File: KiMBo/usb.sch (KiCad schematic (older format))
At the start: 19 parts, among them U1 OSD3358, U6 TPS2051B, U7 TPD4S012, U8 74LVC2G241, U9 TPD4S012

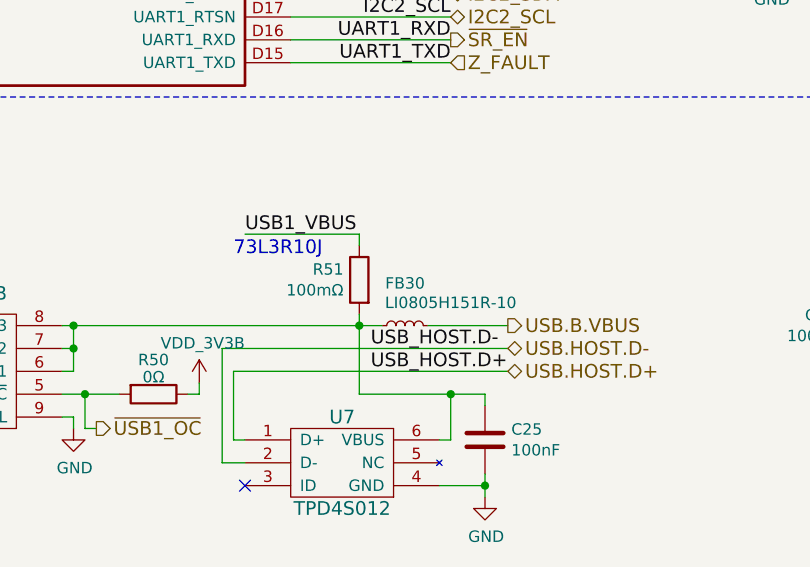
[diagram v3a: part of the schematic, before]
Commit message: Route 24V to the buck, add PTC fuse to 5V output
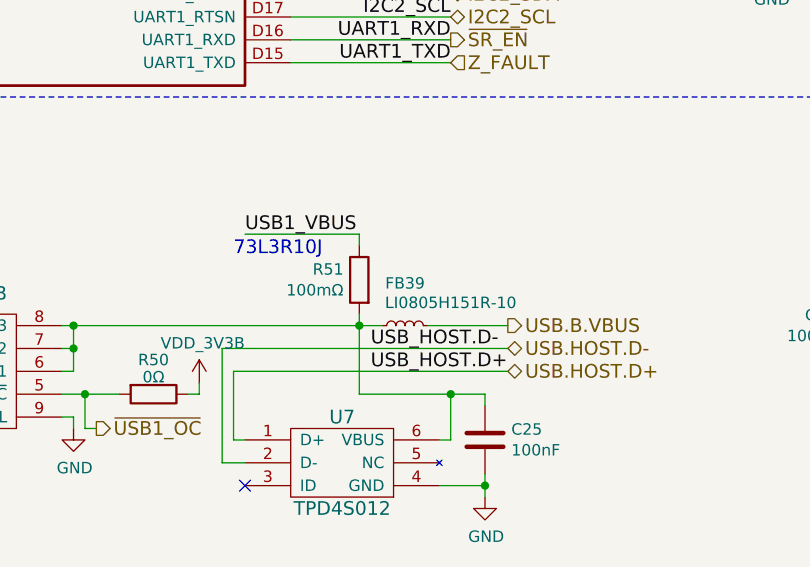
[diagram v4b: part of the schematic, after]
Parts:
- renumbered FB30 to FB39
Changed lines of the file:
@@
 USB.CLIENT.ID
 $Comp
-L INDUCTOR_Small FB30
+L INDUCTOR_Small FB39
 U 1 1 58E84972
 P 5950 4100
-F 0 "FB30" V 6135 4100 50  0000 C CNN
+F 0 "FB39" V 6135 4100 50  0000 C CNN
 F 1 "LI0805H151R-10" V 6050 3900 50  0000 C CNN
 F 2 "Resistors_SMD:R_0805" H 5950 4100 50  0001 C CNN

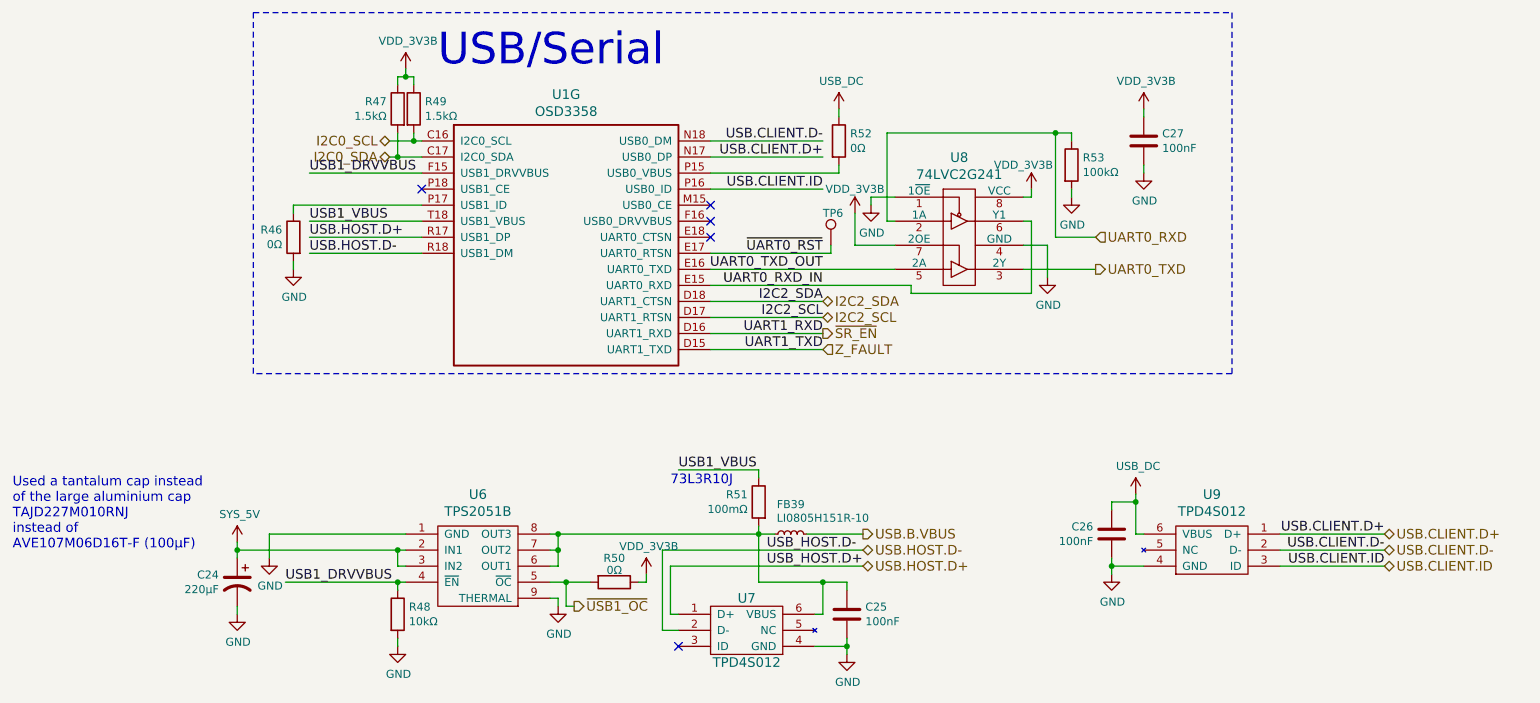
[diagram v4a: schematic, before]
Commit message: Add ferrite beads to the 5V and 3V pins at the SPI connectors
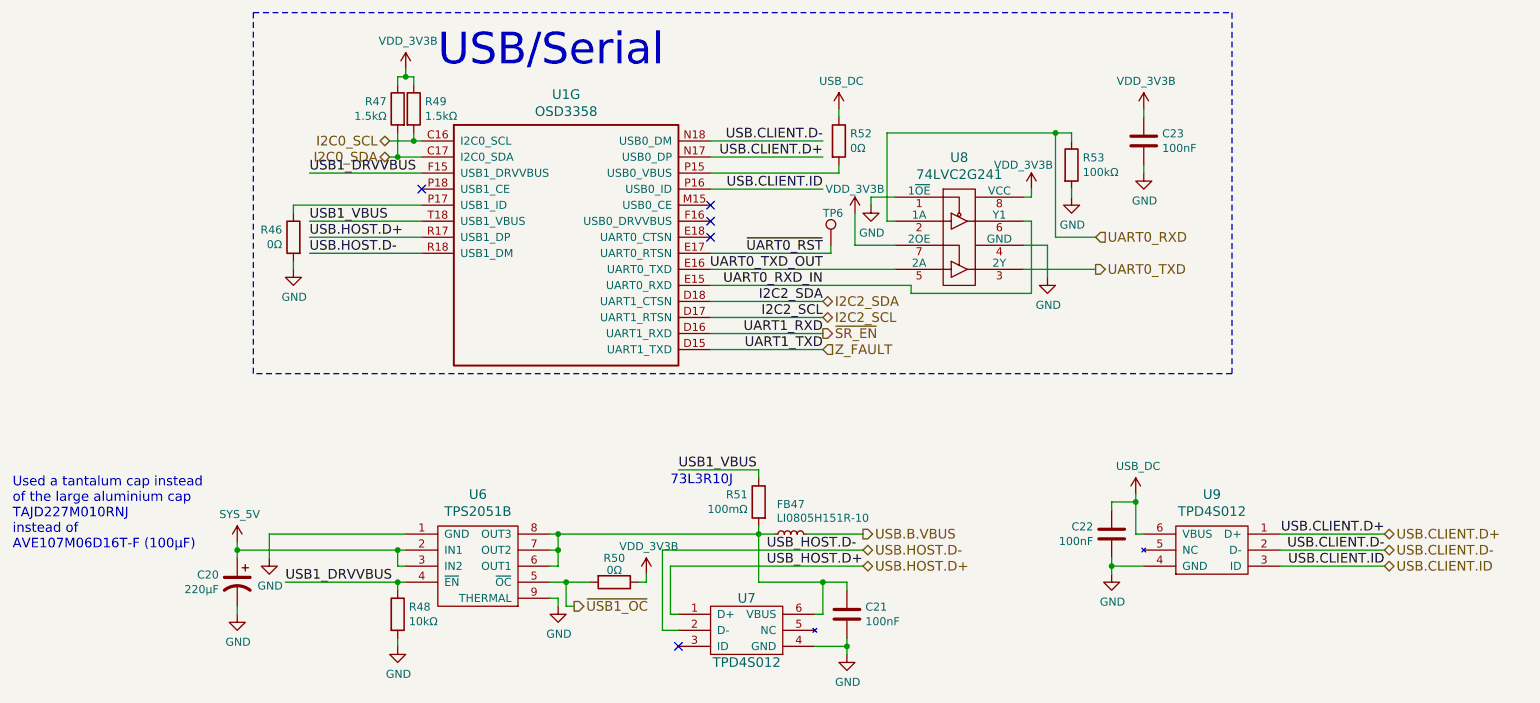
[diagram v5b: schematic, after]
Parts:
- renumbered C24 to C20, C25 to C21, C26 to C22, C27 to C23, FB39 to FB47
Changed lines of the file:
@@
 $EndComp
 $Comp
-L GND #PWR0100
+L GND #PWR097
 U 1 1 584F5078
 P 7550 2500
-F 0 "#PWR0100" H 7550 2250 50  0001 C CNN
+F 0 "#PWR097" H 7550 2250 50  0001 C CNN
 F 1 "GND" H 7555 2327 50  0000 C CNN
 F 2 "" H 7550 2500 50  0000 C CNN
@@
 $EndComp
 $Comp
-L GND #PWR0101
+L GND #PWR098
 U 1 1 584F508C
 P 6450 2050
-F 0 "#PWR0101" H 6450 1800 50  0001 C CNN
+F 0 "#PWR098" H 6450 1800 50  0001 C CNN
 F 1 "GND" H 6455 1877 50  0000 C CNN
 F 2 "" H 6450 2050 50  0000 C CNN
@@
 UART0_TXD_OUT
 $Comp
-L GND #PWR0102
+L GND #PWR099
 U 1 1 584F509A
 P 7700 2000
-F 0 "#PWR0102" H 7700 1750 50  0001 C CNN
+F 0 "#PWR099" H 7700 1750 50  0001 C CNN
 F 1 "GND" H 7705 1827 50  0000 C CNN
 F 2 "" H 7700 2000 50  0000 C CNN
@@
 $EndComp
 $Comp
-L C C27
+L C C23
 U 1 1 584F50A3
 P 8150 1650
-F 0 "C27" H 8265 1696 50  0000 L CNN
+F 0 "C23" H 8265 1696 50  0000 L CNN
 F 1 "100nF" H 8265 1605 50  0000 L CNN
 F 2 "Capacitors_SMD:C_0603" H 8150 1650 50  0001 C CNN
@@
 $EndComp
 $Comp
-L GND #PWR0103
+L GND #PWR0100
 U 1 1 584F50AA
 P 8150 1850
-F 0 "#PWR0103" H 8150 1600 50  0001 C CNN
+F 0 "#PWR0100" H 8150 1600 50  0001 C CNN
 F 1 "GND" H 8155 1677 50  0000 C CNN
 F 2 "" H 8150 1850 50  0000 C CNN
@@
 $EndComp
 $Comp
-L GND #PWR0104
+L GND #PWR0101
 U 1 1 584F50D8
 P 2850 2450
-F 0 "#PWR0104" H 2850 2200 50  0001 C CNN
+F 0 "#PWR0101" H 2850 2200 50  0001 C CNN
 F 1 "GND" H 2855 2277 50  0000 C CNN
 F 2 "" H 2850 2450 50  0000 C CNN
@@
 $EndComp
 $Comp
-L C C25
+L C C21
 U 1 1 58524285
 P 6300 4600
-F 0 "C25" H 6415 4646 50  0000 L CNN
+F 0 "C21" H 6415 4646 50  0000 L CNN
 F 1 "100nF" H 6415 4555 50  0000 L CNN
 F 2 "Capacitors_SMD:C_0603" H 6300 4600 50  0001 C CNN
@@
 $EndComp
 $Comp
-L GND #PWR0105
+L GND #PWR0102
 U 1 1 585243B8
 P 6300 4850
-F 0 "#PWR0105" H 6300 4600 50  0001 C CNN
+F 0 "#PWR0102" H 6300 4600 50  0001 C CNN
 F 1 "GND" H 6305 4677 50  0000 C CNN
 F 2 "" H 6300 4850 50  0000 C CNN
@@
 $EndComp
 $Comp
-L GND #PWR0106
+L GND #PWR0103
 U 1 1 58528602
 P 4500 4550
-F 0 "#PWR0106" H 4500 4300 50  0001 C CNN
+F 0 "#PWR0103" H 4500 4300 50  0001 C CNN
 F 1 "GND" H 4505 4377 50  0000 C CNN
 F 2 "" H 4500 4550 50  0000 C CNN
@@
 $EndComp
 $Comp
-L GND #PWR0107
+L GND #PWR0104
 U 1 1 5852A6BE
 P 2500 4600
-F 0 "#PWR0107" H 2500 4350 50  0001 C CNN
+F 0 "#PWR0104" H 2500 4350 50  0001 C CNN
 F 1 "GND" H 2505 4427 50  0000 C CNN
 F 2 "" H 2500 4600 50  0000 C CNN
@@
 $EndComp
 $Comp
-L GND #PWR0108
+L GND #PWR0105
 U 1 1 5852A82F
 P 2700 4250
-F 0 "#PWR0108" H 2700 4000 50  0001 C CNN
+F 0 "#PWR0105" H 2700 4000 50  0001 C CNN
 F 1 "GND" H 2705 4077 50  0000 C CNN
 F 2 "" H 2700 4250 50  0000 C CNN
@@
 $EndComp
 $Comp
-L GND #PWR0109
+L GND #PWR0106
 U 1 1 5852B68C
 P 3500 4800
-F 0 "#PWR0109" H 3500 4550 50  0001 C CNN
+F 0 "#PWR0106" H 3500 4550 50  0001 C CNN
 F 1 "GND" H 3505 4627 50  0000 C CNN
 F 2 "" H 3500 4800 50  0000 C CNN
@@
 $EndComp
 $Comp
-L C C26
+L C C22
 U 1 1 5852C2E6
 P 7950 4100
-F 0 "C26" H 8065 4146 50  0000 L CNN
+F 0 "C22" H 8065 4146 50  0000 L CNN
 F 1 "100nF" H 8065 4055 50  0000 L CNN
 F 2 "Capacitors_SMD:C_0603" H 7950 4100 50  0001 C CNN
@@
 USB.CLIENT.ID
 $Comp
-L INDUCTOR_Small FB39
+L INDUCTOR_Small FB47
 U 1 1 58E84972
 P 5950 4100
-F 0 "FB39" V 6135 4100 50  0000 C CNN
+F 0 "FB47" V 6135 4100 50  0000 C CNN
 F 1 "LI0805H151R-10" V 6050 3900 50  0000 C CNN
 F 2 "Resistors_SMD:R_0805" H 5950 4100 50  0001 C CNN
@@
 I2C2_SDA
 $Comp
-L USB_DC #PWR0110
+L USB_DC #PWR0107
 U 1 1 59F94F9A
 P 8100 3850
-F 0 "#PWR0110" H 8100 3700 50  0001 C CNN
+F 0 "#PWR0107" H 8100 3700 50  0001 C CNN
 F 1 "USB_DC" H 8115 4023 50  0000 C CNN
 F 2 "" H 8100 3850 50  0000 C CNN
@@
 $EndComp
 $Comp
-L SYS_5V #PWR0111
+L SYS_5V #PWR0108
 U 1 1 59F970D0
 P 2500 4150
-F 0 "#PWR0111" H 2500 4000 50  0001 C CNN
+F 0 "#PWR0108" H 2500 4000 50  0001 C CNN
 F 1 "SYS_5V" H 2515 4323 50  0000 C CNN
 F 2 "" H 2500 4150 50  0000 C CNN
@@
 $EndComp
 $Comp
-L VDD_3V3B #PWR0112
+L VDD_3V3B #PWR0109
 U 1 1 59FBF8B1
 P 6350 2100
-F 0 "#PWR0112" H 6350 1950 50  0001 C CNN
+F 0 "#PWR0109" H 6350 1950 50  0001 C CNN
 F 1 "VDD_3V3B" H 6350 2250 50  0000 C CNN
 F 2 "" H 6350 2100 50  0000 C CNN
@@
 $EndComp
 $Comp
-L VDD_3V3B #PWR0113
+L VDD_3V3B #PWR0110
 U 1 1 59FBF8FC
 P 7450 1950
-F 0 "#PWR0113" H 7450 1800 50  0001 C CNN
+F 0 "#PWR0110" H 7450 1800 50  0001 C CNN
 F 1 "VDD_3V3B" H 7400 2100 50  0000 C CNN
 F 2 "" H 7450 1950 50  0000 C CNN
@@
 $EndComp
 $Comp
-L VDD_3V3B #PWR0114
+L VDD_3V3B #PWR0111
 U 1 1 59FC0162
 P 8150 1450
-F 0 "#PWR0114" H 8150 1300 50  0001 C CNN
+F 0 "#PWR0111" H 8150 1300 50  0001 C CNN
 F 1 "VDD_3V3B" H 8165 1623 50  0000 C CNN
 F 2 "" H 8150 1450 50  0000 C CNN
@@
 $EndComp
 $Comp
-L USB_DC #PWR0115
+L USB_DC #PWR0112
 U 1 1 59FEDDB0
 P 6250 1450
-F 0 "#PWR0115" H 6250 1300 50  0001 C CNN
+F 0 "#PWR0112" H 6250 1300 50  0001 C CNN
 F 1 "USB_DC" H 6265 1623 50  0000 C CNN
 F 2 "" H 6250 1450 50  0000 C CNN
@@
 $EndComp
 $Comp
-L VDD_3V3B #PWR0116
+L VDD_3V3B #PWR0113
 U 1 1 5A01DA26
 P 3550 1200
-F 0 "#PWR0116" H 3550 1050 50  0001 C CNN
+F 0 "#PWR0113" H 3550 1050 50  0001 C CNN
 F 1 "VDD_3V3B" H 3565 1373 50  0000 C CNN
 F 2 "" H 3550 1200 50  0000 C CNN
@@
 Used a tantalum cap instead\nof the large aluminium cap\nTAJD227M010RNJ\ninstead of\nAVE107M06D16T-F (100μF)
 $Comp
-L VDD_3V3B #PWR0117
+L VDD_3V3B #PWR0114
 U 1 1 5AF563FC
 P 5050 4350
-F 0 "#PWR0117" H 5050 4200 50  0001 C CNN
+F 0 "#PWR0114" H 5050 4200 50  0001 C CNN
 F 1 "VDD_3V3B" H 5065 4523 50  0000 C CNN
 F 2 "" H 5050 4350 50  0000 C CNN
@@
 $EndComp
 $Comp
-L GND #PWR0118
+L GND #PWR0115
 U 1 1 5BC77EEA
 P 7950 4350
-F 0 "#PWR0118" H 7950 4100 50  0001 C CNN
+F 0 "#PWR0115" H 7950 4100 50  0001 C CNN
 F 1 "GND" H 7955 4177 50  0000 C CNN
 F 2 "" H 7950 4350 50  0000 C CNN
@@
 73L3R10J
 $Comp
-L CP1 C24
+L CP1 C20
 U 1 1 58EB0DF2
 P 2500 4400
-F 0 "C24" H 2615 4446 50  0000 L CNN
+F 0 "C20" H 2615 4446 50  0000 L CNN
 F 1 "220μF" H 2615 4355 50  0000 L CNN
 F 2 "Capacitors_Tantalum_SMD:TantalC_SizeD_EIA-7343_Reflow" H 2500 4400 50  0001 C CNN

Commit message: Complete SPI, ADC, and Endstop header layout/position, add zone around the SiP
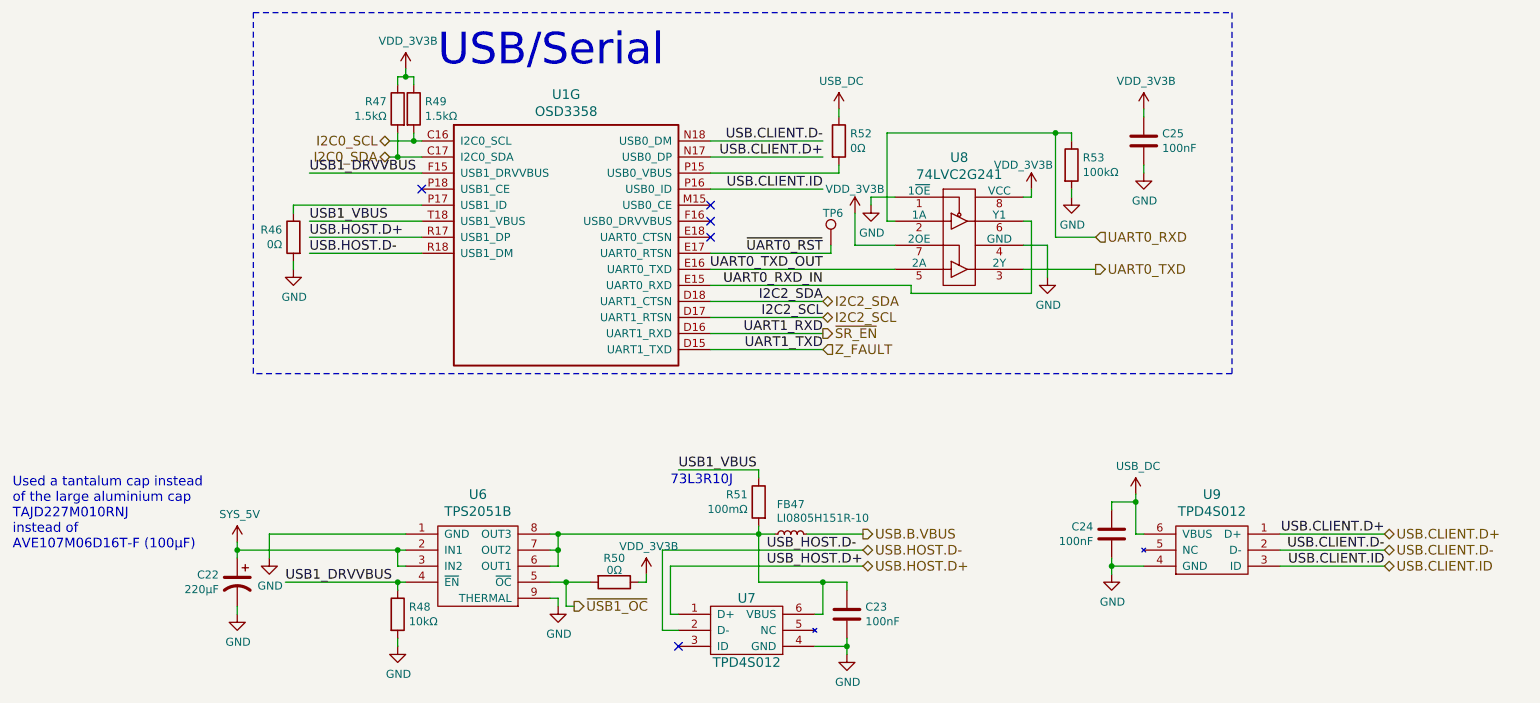
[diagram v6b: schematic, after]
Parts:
- renumbered C20 to C22, C21 to C23, C22 to C24, C23 to C25
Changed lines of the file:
@@
 $EndComp
 $Comp
-L GND #PWR097
+L GND #PWR099
 U 1 1 584F5078
 P 7550 2500
-F 0 "#PWR097" H 7550 2250 50  0001 C CNN
+F 0 "#PWR099" H 7550 2250 50  0001 C CNN
 F 1 "GND" H 7555 2327 50  0000 C CNN
 F 2 "" H 7550 2500 50  0000 C CNN
@@
 $EndComp
 $Comp
-L GND #PWR098
+L GND #PWR0100
 U 1 1 584F508C
 P 6450 2050
-F 0 "#PWR098" H 6450 1800 50  0001 C CNN
+F 0 "#PWR0100" H 6450 1800 50  0001 C CNN
 F 1 "GND" H 6455 1877 50  0000 C CNN
 F 2 "" H 6450 2050 50  0000 C CNN
@@
 UART0_TXD_OUT
 $Comp
-L GND #PWR099
+L GND #PWR0101
 U 1 1 584F509A
 P 7700 2000
-F 0 "#PWR099" H 7700 1750 50  0001 C CNN
+F 0 "#PWR0101" H 7700 1750 50  0001 C CNN
 F 1 "GND" H 7705 1827 50  0000 C CNN
 F 2 "" H 7700 2000 50  0000 C CNN
@@
 $EndComp
 $Comp
-L C C23
+L C C25
 U 1 1 584F50A3
 P 8150 1650
-F 0 "C23" H 8265 1696 50  0000 L CNN
+F 0 "C25" H 8265 1696 50  0000 L CNN
 F 1 "100nF" H 8265 1605 50  0000 L CNN
 F 2 "Capacitors_SMD:C_0603" H 8150 1650 50  0001 C CNN
@@
 $EndComp
 $Comp
-L GND #PWR0100
+L GND #PWR0102
 U 1 1 584F50AA
 P 8150 1850
-F 0 "#PWR0100" H 8150 1600 50  0001 C CNN
+F 0 "#PWR0102" H 8150 1600 50  0001 C CNN
 F 1 "GND" H 8155 1677 50  0000 C CNN
 F 2 "" H 8150 1850 50  0000 C CNN
@@
 $EndComp
 $Comp
-L GND #PWR0101
+L GND #PWR0103
 U 1 1 584F50D8
 P 2850 2450
-F 0 "#PWR0101" H 2850 2200 50  0001 C CNN
+F 0 "#PWR0103" H 2850 2200 50  0001 C CNN
 F 1 "GND" H 2855 2277 50  0000 C CNN
 F 2 "" H 2850 2450 50  0000 C CNN
@@
 $EndComp
 $Comp
-L C C21
+L C C23
 U 1 1 58524285
 P 6300 4600
-F 0 "C21" H 6415 4646 50  0000 L CNN
+F 0 "C23" H 6415 4646 50  0000 L CNN
 F 1 "100nF" H 6415 4555 50  0000 L CNN
 F 2 "Capacitors_SMD:C_0603" H 6300 4600 50  0001 C CNN
@@
 $EndComp
 $Comp
-L GND #PWR0102
+L GND #PWR0104
 U 1 1 585243B8
 P 6300 4850
-F 0 "#PWR0102" H 6300 4600 50  0001 C CNN
+F 0 "#PWR0104" H 6300 4600 50  0001 C CNN
 F 1 "GND" H 6305 4677 50  0000 C CNN
 F 2 "" H 6300 4850 50  0000 C CNN
@@
 $EndComp
 $Comp
-L GND #PWR0103
+L GND #PWR0105
 U 1 1 58528602
 P 4500 4550
-F 0 "#PWR0103" H 4500 4300 50  0001 C CNN
+F 0 "#PWR0105" H 4500 4300 50  0001 C CNN
 F 1 "GND" H 4505 4377 50  0000 C CNN
 F 2 "" H 4500 4550 50  0000 C CNN
@@
 $EndComp
 $Comp
-L GND #PWR0104
+L GND #PWR0106
 U 1 1 5852A6BE
 P 2500 4600
-F 0 "#PWR0104" H 2500 4350 50  0001 C CNN
+F 0 "#PWR0106" H 2500 4350 50  0001 C CNN
 F 1 "GND" H 2505 4427 50  0000 C CNN
 F 2 "" H 2500 4600 50  0000 C CNN
@@
 $EndComp
 $Comp
-L GND #PWR0105
+L GND #PWR0107
 U 1 1 5852A82F
 P 2700 4250
-F 0 "#PWR0105" H 2700 4000 50  0001 C CNN
+F 0 "#PWR0107" H 2700 4000 50  0001 C CNN
 F 1 "GND" H 2705 4077 50  0000 C CNN
 F 2 "" H 2700 4250 50  0000 C CNN
@@
 $EndComp
 $Comp
-L GND #PWR0106
+L GND #PWR0108
 U 1 1 5852B68C
 P 3500 4800
-F 0 "#PWR0106" H 3500 4550 50  0001 C CNN
+F 0 "#PWR0108" H 3500 4550 50  0001 C CNN
 F 1 "GND" H 3505 4627 50  0000 C CNN
 F 2 "" H 3500 4800 50  0000 C CNN
@@
 $EndComp
 $Comp
-L C C22
+L C C24
 U 1 1 5852C2E6
 P 7950 4100
-F 0 "C22" H 8065 4146 50  0000 L CNN
+F 0 "C24" H 8065 4146 50  0000 L CNN
 F 1 "100nF" H 8065 4055 50  0000 L CNN
 F 2 "Capacitors_SMD:C_0603" H 7950 4100 50  0001 C CNN
@@
 I2C2_SDA
 $Comp
-L USB_DC #PWR0107
+L USB_DC #PWR0109
 U 1 1 59F94F9A
 P 8100 3850
-F 0 "#PWR0107" H 8100 3700 50  0001 C CNN
+F 0 "#PWR0109" H 8100 3700 50  0001 C CNN
 F 1 "USB_DC" H 8115 4023 50  0000 C CNN
 F 2 "" H 8100 3850 50  0000 C CNN
@@
 $EndComp
 $Comp
-L SYS_5V #PWR0108
+L SYS_5V #PWR0110
 U 1 1 59F970D0
 P 2500 4150
-F 0 "#PWR0108" H 2500 4000 50  0001 C CNN
+F 0 "#PWR0110" H 2500 4000 50  0001 C CNN
 F 1 "SYS_5V" H 2515 4323 50  0000 C CNN
 F 2 "" H 2500 4150 50  0000 C CNN
@@
 $EndComp
 $Comp
-L VDD_3V3B #PWR0109
+L VDD_3V3B #PWR0111
 U 1 1 59FBF8B1
 P 6350 2100
-F 0 "#PWR0109" H 6350 1950 50  0001 C CNN
+F 0 "#PWR0111" H 6350 1950 50  0001 C CNN
 F 1 "VDD_3V3B" H 6350 2250 50  0000 C CNN
 F 2 "" H 6350 2100 50  0000 C CNN
@@
 $EndComp
 $Comp
-L VDD_3V3B #PWR0110
+L VDD_3V3B #PWR0112
 U 1 1 59FBF8FC
 P 7450 1950
-F 0 "#PWR0110" H 7450 1800 50  0001 C CNN
+F 0 "#PWR0112" H 7450 1800 50  0001 C CNN
 F 1 "VDD_3V3B" H 7400 2100 50  0000 C CNN
 F 2 "" H 7450 1950 50  0000 C CNN
@@
 $EndComp
 $Comp
-L VDD_3V3B #PWR0111
+L VDD_3V3B #PWR0113
 U 1 1 59FC0162
 P 8150 1450
-F 0 "#PWR0111" H 8150 1300 50  0001 C CNN
+F 0 "#PWR0113" H 8150 1300 50  0001 C CNN
 F 1 "VDD_3V3B" H 8165 1623 50  0000 C CNN
 F 2 "" H 8150 1450 50  0000 C CNN
@@
 $EndComp
 $Comp
-L USB_DC #PWR0112
+L USB_DC #PWR0114
 U 1 1 59FEDDB0
 P 6250 1450
-F 0 "#PWR0112" H 6250 1300 50  0001 C CNN
+F 0 "#PWR0114" H 6250 1300 50  0001 C CNN
 F 1 "USB_DC" H 6265 1623 50  0000 C CNN
 F 2 "" H 6250 1450 50  0000 C CNN
@@
 $EndComp
 $Comp
-L VDD_3V3B #PWR0113
+L VDD_3V3B #PWR0115
 U 1 1 5A01DA26
 P 3550 1200
-F 0 "#PWR0113" H 3550 1050 50  0001 C CNN
+F 0 "#PWR0115" H 3550 1050 50  0001 C CNN
 F 1 "VDD_3V3B" H 3565 1373 50  0000 C CNN
 F 2 "" H 3550 1200 50  0000 C CNN
@@
 Used a tantalum cap instead\nof the large aluminium cap\nTAJD227M010RNJ\ninstead of\nAVE107M06D16T-F (100μF)
 $Comp
-L VDD_3V3B #PWR0114
+L VDD_3V3B #PWR0116
 U 1 1 5AF563FC
 P 5050 4350
-F 0 "#PWR0114" H 5050 4200 50  0001 C CNN
+F 0 "#PWR0116" H 5050 4200 50  0001 C CNN
 F 1 "VDD_3V3B" H 5065 4523 50  0000 C CNN
 F 2 "" H 5050 4350 50  0000 C CNN
@@
 $EndComp
 $Comp
-L GND #PWR0115
+L GND #PWR0117
 U 1 1 5BC77EEA
 P 7950 4350
-F 0 "#PWR0115" H 7950 4100 50  0001 C CNN
+F 0 "#PWR0117" H 7950 4100 50  0001 C CNN
 F 1 "GND" H 7955 4177 50  0000 C CNN
 F 2 "" H 7950 4350 50  0000 C CNN
@@
 73L3R10J
 $Comp
-L CP1 C20
+L CP1 C22
 U 1 1 58EB0DF2
 P 2500 4400
-F 0 "C20" H 2615 4446 50  0000 L CNN
+F 0 "C22" H 2615 4446 50  0000 L CNN
 F 1 "220μF" H 2615 4355 50  0000 L CNN
 F 2 "Capacitors_Tantalum_SMD:TantalC_SizeD_EIA-7343_Reflow" H 2500 4400 50  0001 C CNN
